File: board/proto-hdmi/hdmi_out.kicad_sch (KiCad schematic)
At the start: 2 parts

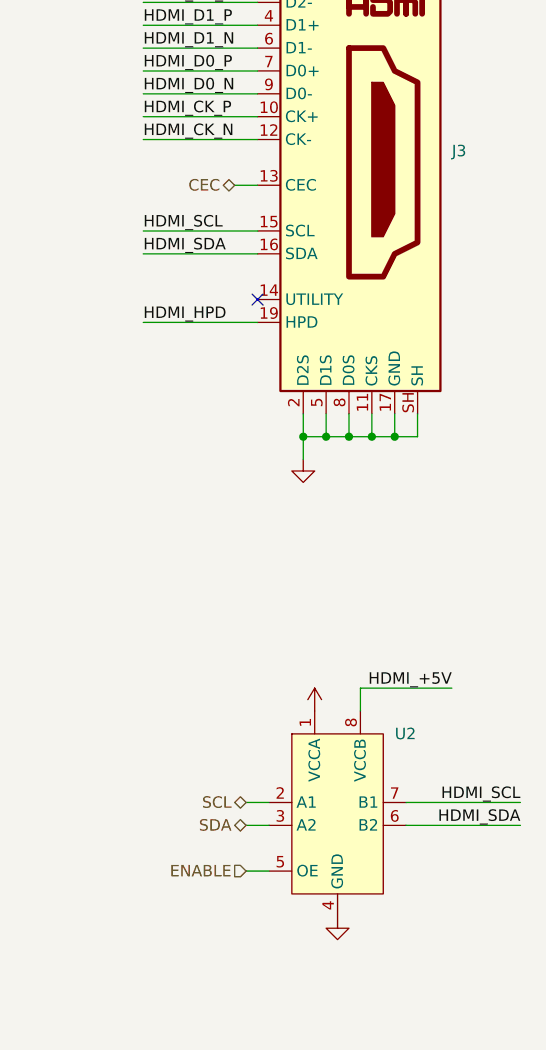
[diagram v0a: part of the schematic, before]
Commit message: Connect source port hotplug detect.
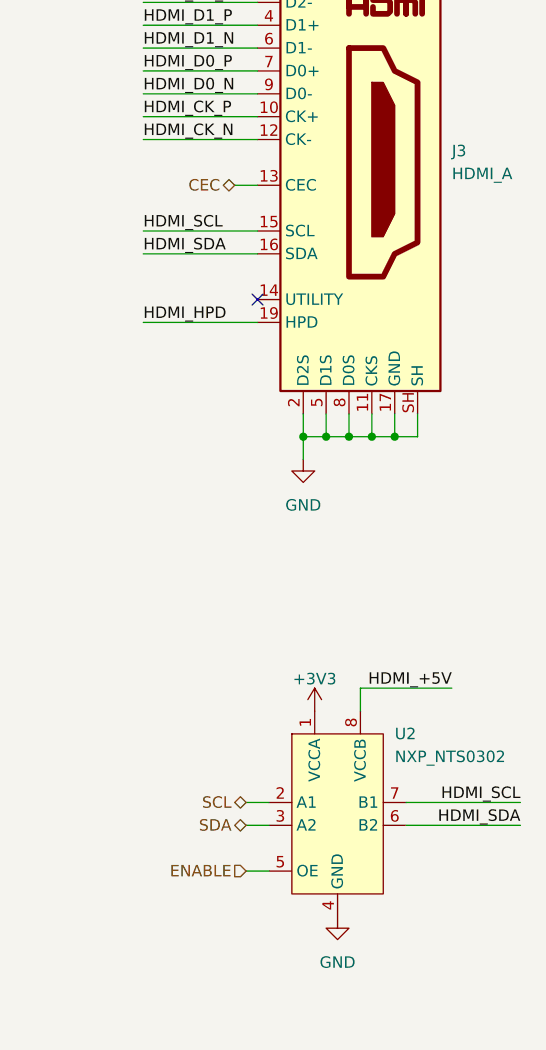
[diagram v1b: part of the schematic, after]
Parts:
- J3: value (none) -> HDMI_A; footprint (none) -> 0Local:CNC_2000-1-2-41-00-BK
- U2: value (none) -> NXP_NTS0302; footprint (none) -> Package_SON:X2SON-8_1.4x1mm_P0.35mm
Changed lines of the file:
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@@
       (effects (font (size 1.27 1.27)) hide)
     )
-    (property "Value" "" (id 1) (at 231.14 114.3 0))
+    (property "Value" "GND" (id 1) (at 231.14 114.3 0))
     (property "Footprint" "" (id 2) (at 231.14 109.22 0)
       (effects (font (size 1.27 1.27)) hide)
@@
       (effects (font (size 1.27 1.27)) (justify left))
     )
-    (property "Value" "" (id 1) (at 241.3 142.24 0)
+    (property "Value" "NXP_NTS0302" (id 1) (at 241.3 142.24 0)
       (effects (font (size 1.27 1.27)) (justify left))
     )
-    (property "Footprint" "" (id 2) (at 234.95 151.13 0)
+    (property "Footprint" "Package_SON:X2SON-8_1.4x1mm_P0.35mm" (id 2) (at 234.95 151.13 0)
       (effects (font (size 1.27 1.27)) hide)
     )
@@
       (effects (font (size 1.27 1.27)) (justify left))
     )
-    (property "Value" "" (id 1) (at 247.65 77.4699 0)
+    (property "Value" "HDMI_A" (id 1) (at 247.65 77.4699 0)
       (effects (font (size 1.27 1.27)) (justify left))
     )
-    (property "Footprint" "" (id 2) (at 236.855 76.2 0)
+    (property "Footprint" "0Local:CNC_2000-1-2-41-00-BK" (id 2) (at 236.855 76.2 0)
       (effects (font (size 1.27 1.27)) hide)
     )
@@
       (effects (font (size 1.27 1.27)) hide)
     )
-    (property "Value" "" (id 1) (at 232.41 133.604 0))
+    (property "Value" "+3V3" (id 1) (at 232.41 133.604 0))
     (property "Footprint" "" (id 2) (at 232.41 137.16 0)
       (effects (font (size 1.27 1.27)) hide)
@@
       (effects (font (size 1.27 1.27)) hide)
     )
-    (property "Value" "" (id 1) (at 234.95 165.1 0))
+    (property "Value" "GND" (id 1) (at 234.95 165.1 0))
     (property "Footprint" "" (id 2) (at 234.95 160.02 0)
       (effects (font (size 1.27 1.27)) hide)

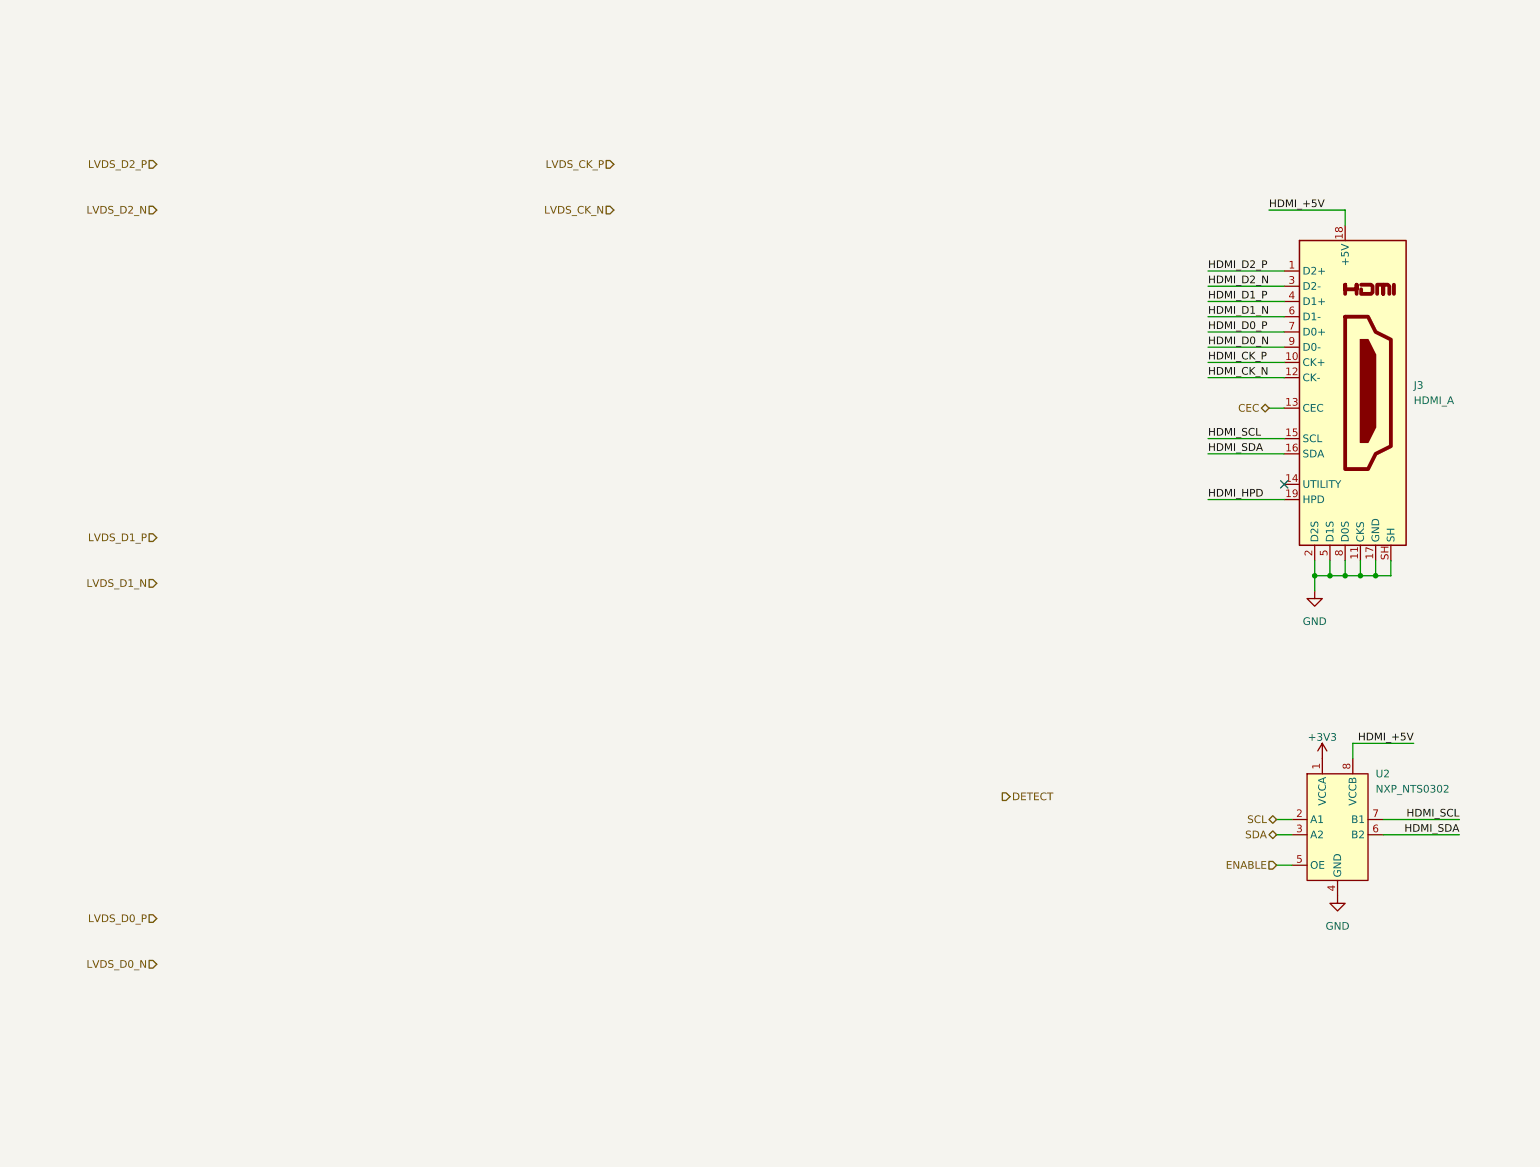
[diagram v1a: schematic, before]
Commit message: Set up most of the non-TMDS source stuff.
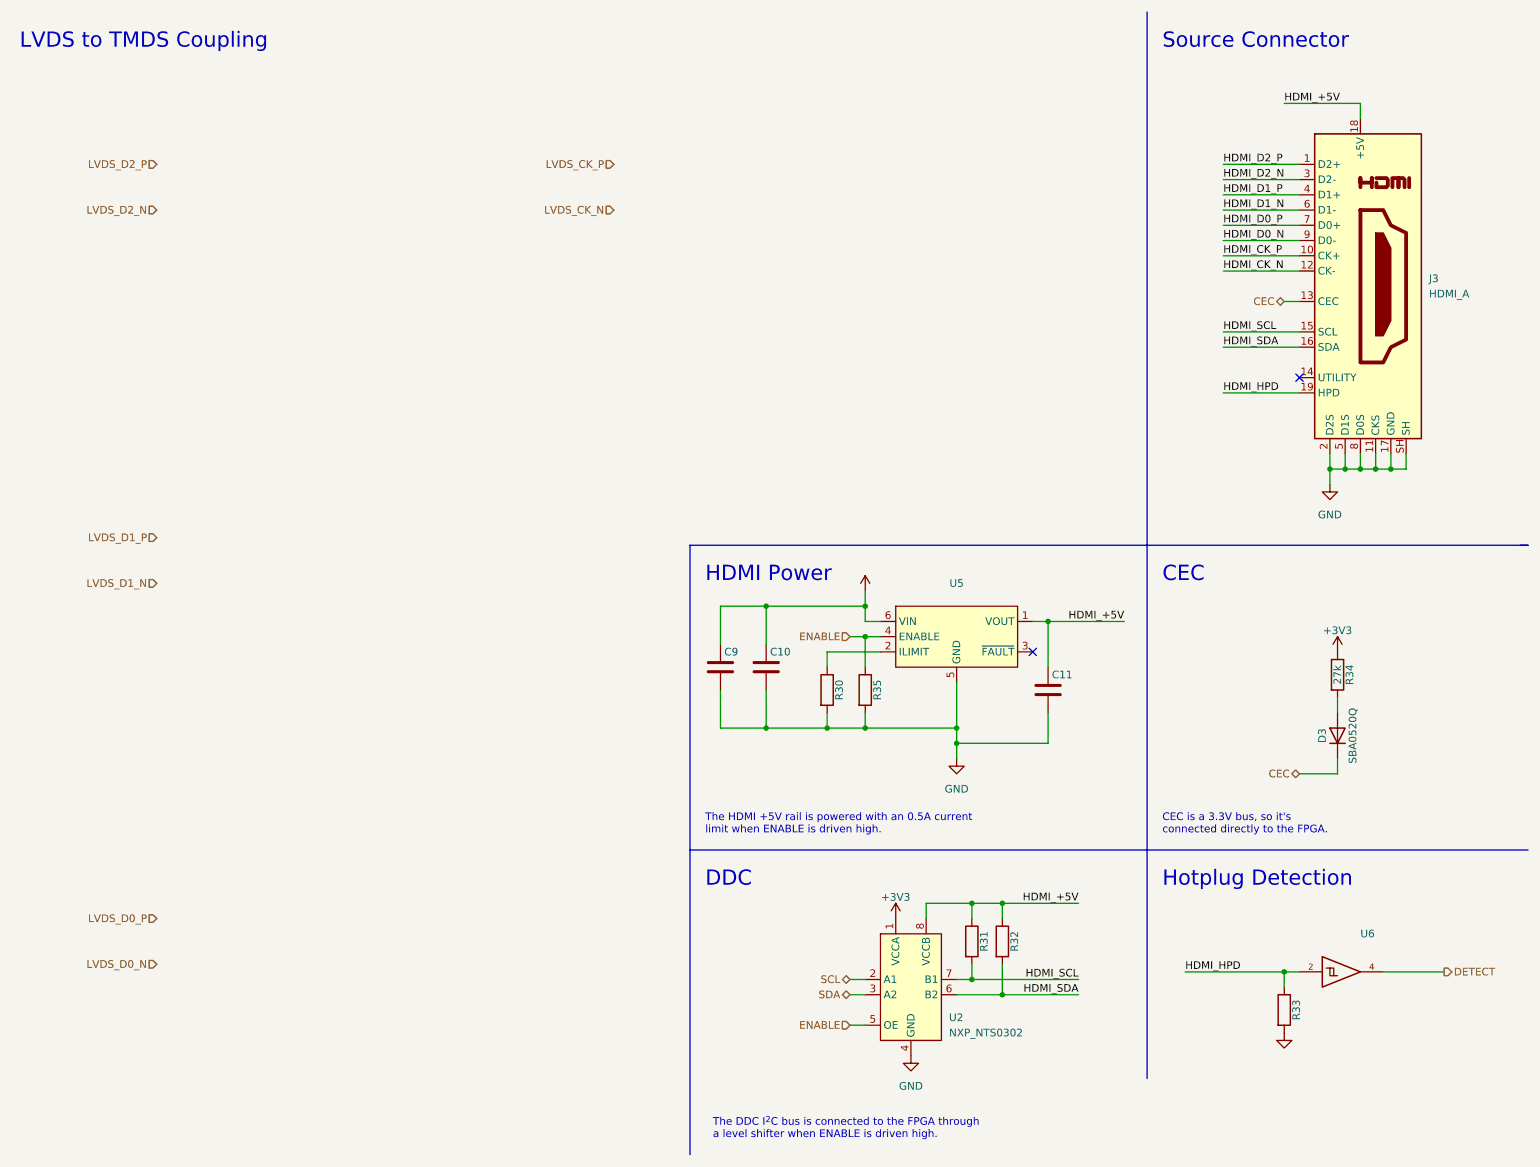
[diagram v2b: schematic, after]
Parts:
- added C10, C11, C9: (no value), symbol Device:C
- added D3: SBA0520Q, Diode_SMD:D_0402_1005Metric, symbol Device:D
- added R30, R31, R32, R33, R35: (no value), symbol Device:R
- added R34: 27k, Resistor_SMD:R_0402_1005Metric, symbol Device:R
- added U5: (no value), 0Local:Package_TMLF-6_EP_1.6mm, symbol 0Local:MIC2097-1
- added U6: (no value), symbol 74xGxx:74LVC1G17
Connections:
- net +3V3: now also R34.1
- net CEC: now also D3.1 (K)
- net DETECT: now also U6.4
- net ENABLE: now also R35.1, U5.4 (ENABLE)
- net HDMI_+5V: now also C11.1, R31.1, R32.1, U5.1 (VOUT)
- net HDMI_HPD: now also R33.1, U6.2
- net HDMI_SCL: now also R31.2
- net HDMI_SDA: now also R32.2
- net GND renamed EP
- net EP: now also C10.2, C11.2, C9.2, R30.2, R33.2, R35.2, U5.5 (GND), U5.EP, U6.3 (GND)
- new net: D3.2 (A), R34.2
- new net: R30.1, U5.2 (ILIMIT)
- new net +5V: C10.1, C9.1, U5.6 (VIN)
- new net VCC: U6.5 (VCC)
- no-connect marks 1 -> 2
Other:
- note added: "CEC"
- note added: "CEC is a 3.3V bus, so it's connected directly to the FPGA."
- note added: "DDC"
- note added: "HDMI Power"
- note added: "Hotplug Detection"
- note added: "LVDS to TMDS Coupling"
- note added: "Source Connector"
- note added: "The DDC I^{2}C bus is connected to the FPGA through a level shifter when ENABLE is driven high."
- note added: "The HDMI +5V rail is powered with an 0.5A current limit when ENABLE is driven high."
- moved on the sheet: J3, U2

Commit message: Tweak HDMI bits.
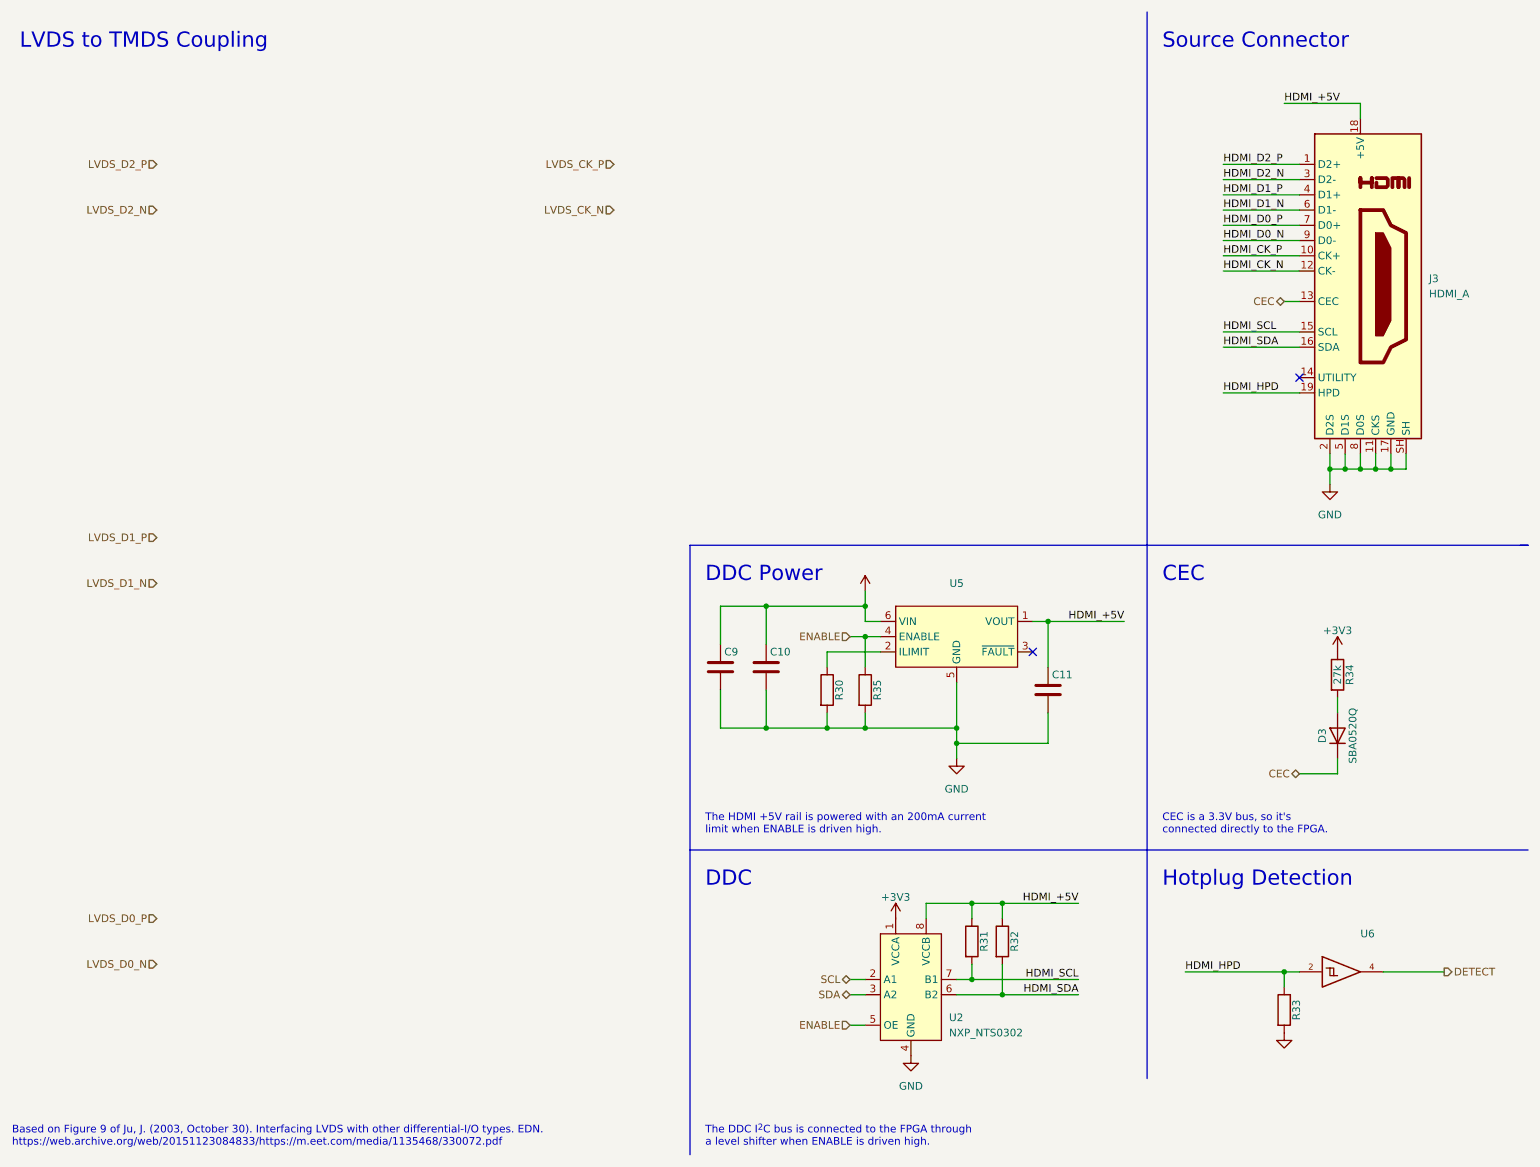
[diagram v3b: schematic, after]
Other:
- note added: "Based on Figure 9 of Ju, J. (2003, October 30). Interfacing LVDS with other differential-I/O types. EDN. https://web.archive.org/web/20151123084833/https://m.eet.com/media/1135468/330072.pdf"
- note added: "DDC Power"
- note added: "The HDMI +5V rail is powered with an 200mA current limit when ENABLE is driven high."
- note removed: "HDMI Power"
- note removed: "The HDMI +5V rail is powered with an 0.5A current limit when ENABLE is driven high."
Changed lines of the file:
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@@
     (effects (font (size 2.54 2.54)) (justify left bottom))
+  )
+  (text "Based on Figure 9 of Ju, J. (2003, October 30). Interfacing LVDS with other differential-I/O types. EDN.\nhttps://web.archive.org/web/20151123084833/https://m.eet.com/media/1135468/330072.pdf"
+    (at 13.97 201.93 0)
+    (effects (font (size 1.27 1.27)) (justify left bottom))
   )
   (text "Hotplug Detection" (at 205.74 158.75 0)
@@
     (effects (font (size 2.54 2.54)) (justify left bottom))
   )
-  (text "HDMI Power" (at 129.54 107.95 0)
+  (text "DDC Power" (at 129.54 107.95 0)
     (effects (font (size 2.54 2.54)) (justify left bottom))
   )
@@
     (effects (font (size 2.54 2.54)) (justify left bottom))
   )
-  (text "The HDMI +5V rail is powered with an 0.5A current\nlimit when ENABLE is driven high."
+  (text "The HDMI +5V rail is powered with an 200mA current\nlimit when ENABLE is driven high."
     (at 129.54 149.86 0)
     (effects (font (size 1.27 1.27)) (justify left bottom))
   )
   (text "The DDC I^{2}C bus is connected to the FPGA through\na level shifter when ENABLE is driven high."
-    (at 130.81 200.66 0)
+    (at 129.54 201.93 0)
     (effects (font (size 1.27 1.27)) (justify left bottom))
   )
